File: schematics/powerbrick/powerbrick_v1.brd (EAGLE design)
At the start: 100 x 80 mm, 39 parts, among them U1 ATXMEGA128C3-AU, U2 TC1262-3.3VDB, U3 PRTR5V0U2X, U4 ULN2003LVPWR, U5 MCP9800A0T-M/OT

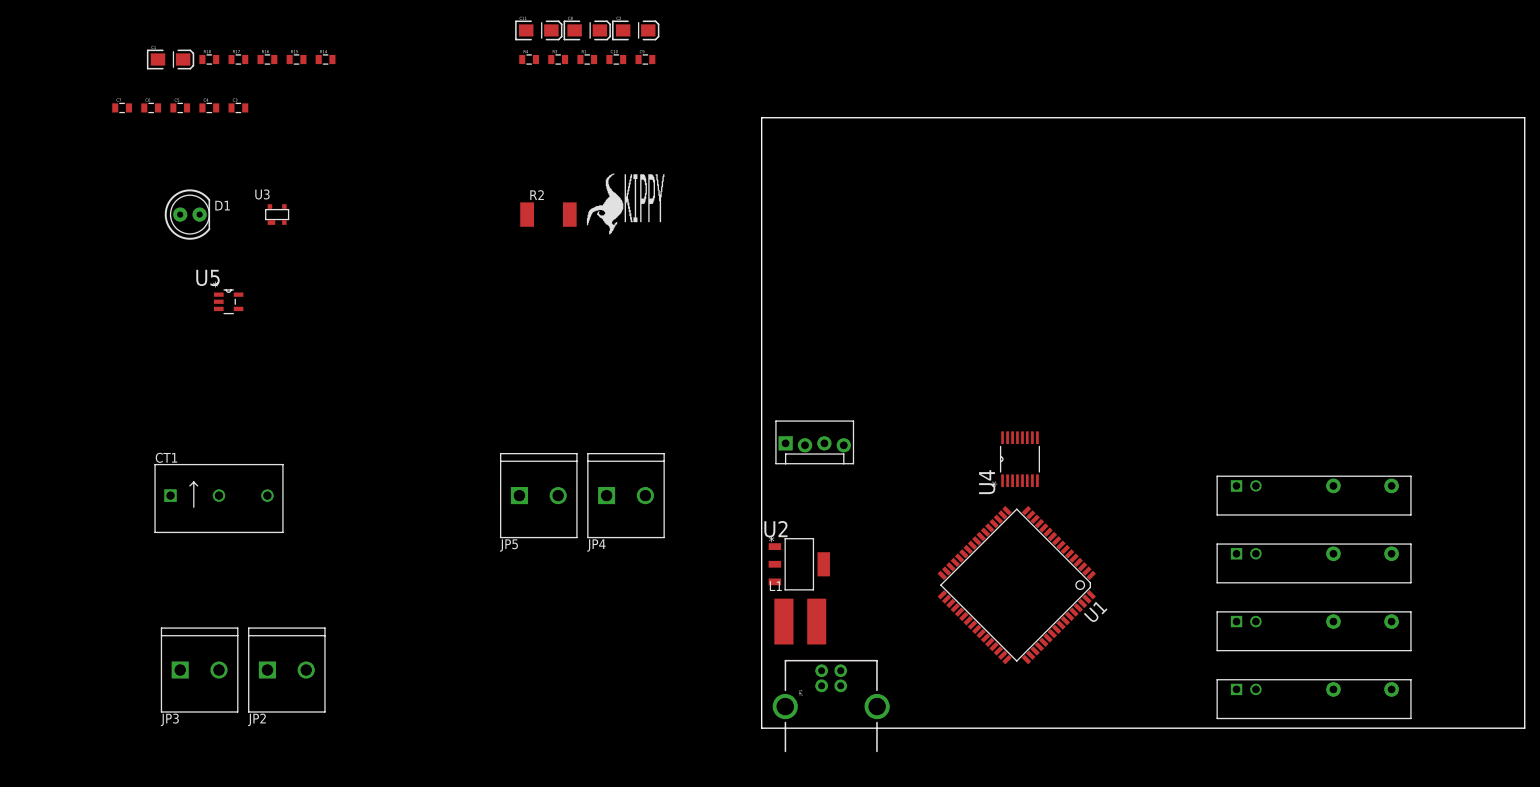
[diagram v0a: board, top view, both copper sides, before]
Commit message: Added ISP header
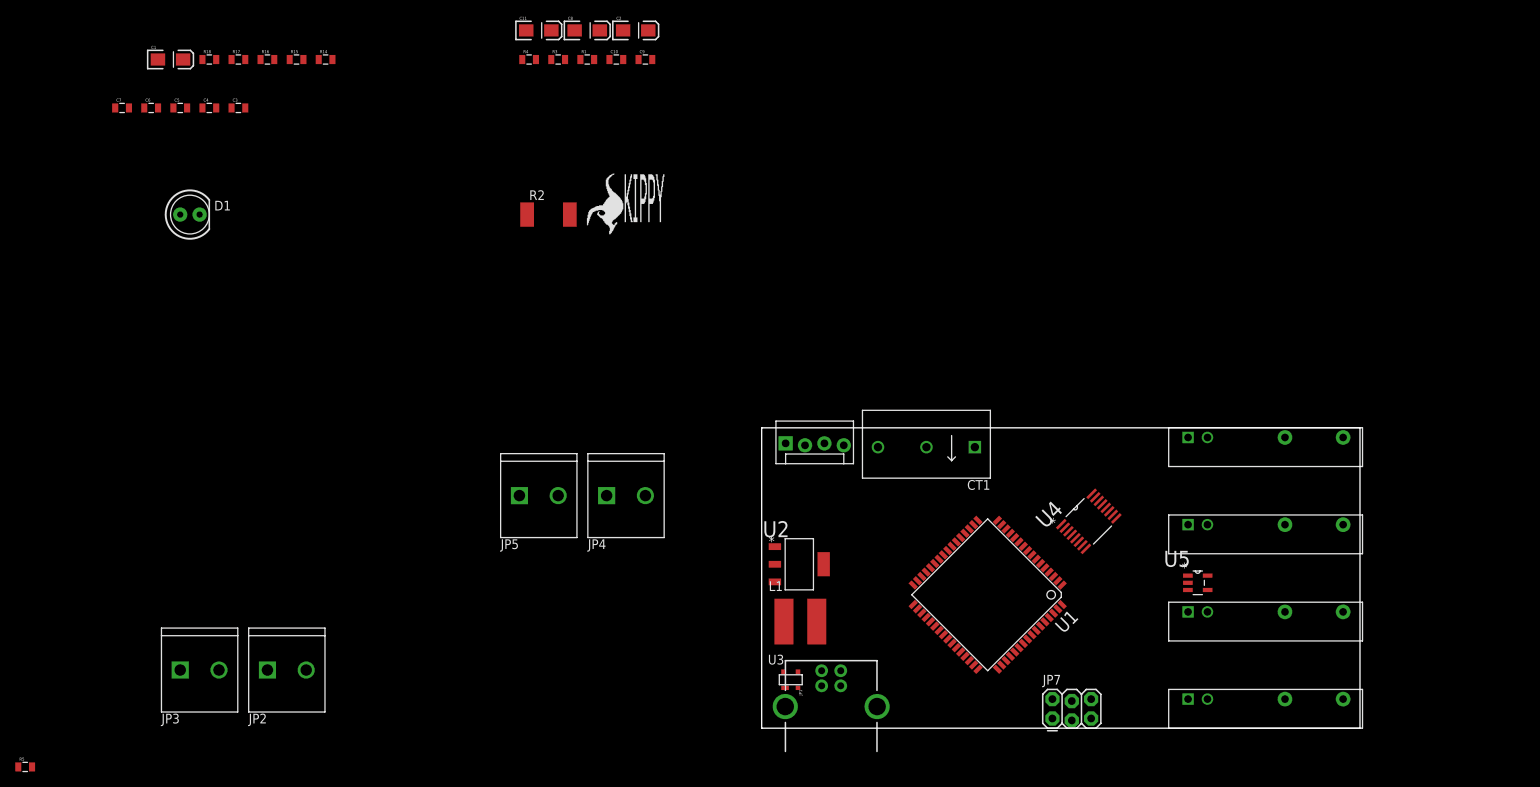
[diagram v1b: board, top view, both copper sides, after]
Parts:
- added JP7: AVR_SPI_PRG_62X3_LOCK, SparkFun-Connectors:2X3_LOCK
- added R5: 10k, SparkFun-Passives:0805
- moved U5 132.2 mm to (57.1, 19.1)
- moved CT1 92.9 mm to (21.6, 36.8), turned to 180 degrees
- moved U3 90.8 mm to (3.81, 6.35)
- moved SSR3 17.7 mm to (66.0, 15.2)
- moved SSR1 16.5 mm to (66.0, 38.1)
- moved SSR2 14.2 mm to (66.0, 26.7)
- moved U4 12.1 mm to (42.9, 27.1), turned to 45 degrees
- moved SSR4 6.48 mm to (66.0, 3.81)
- moved U1 4.02 mm to (29.6, 17.5)
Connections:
- new net PDI_CLK: JP7.5, R5.2, U1.57
- new net PDI_DATA: JP7.1, U1.56
- net 3.3V: now also JP7.2, R5.1
- net GND: now also JP7.6
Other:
- board size 100 x 80 mm -> 78.4 x 39.4 mm

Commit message: Replaced ISP connector - PCB draft
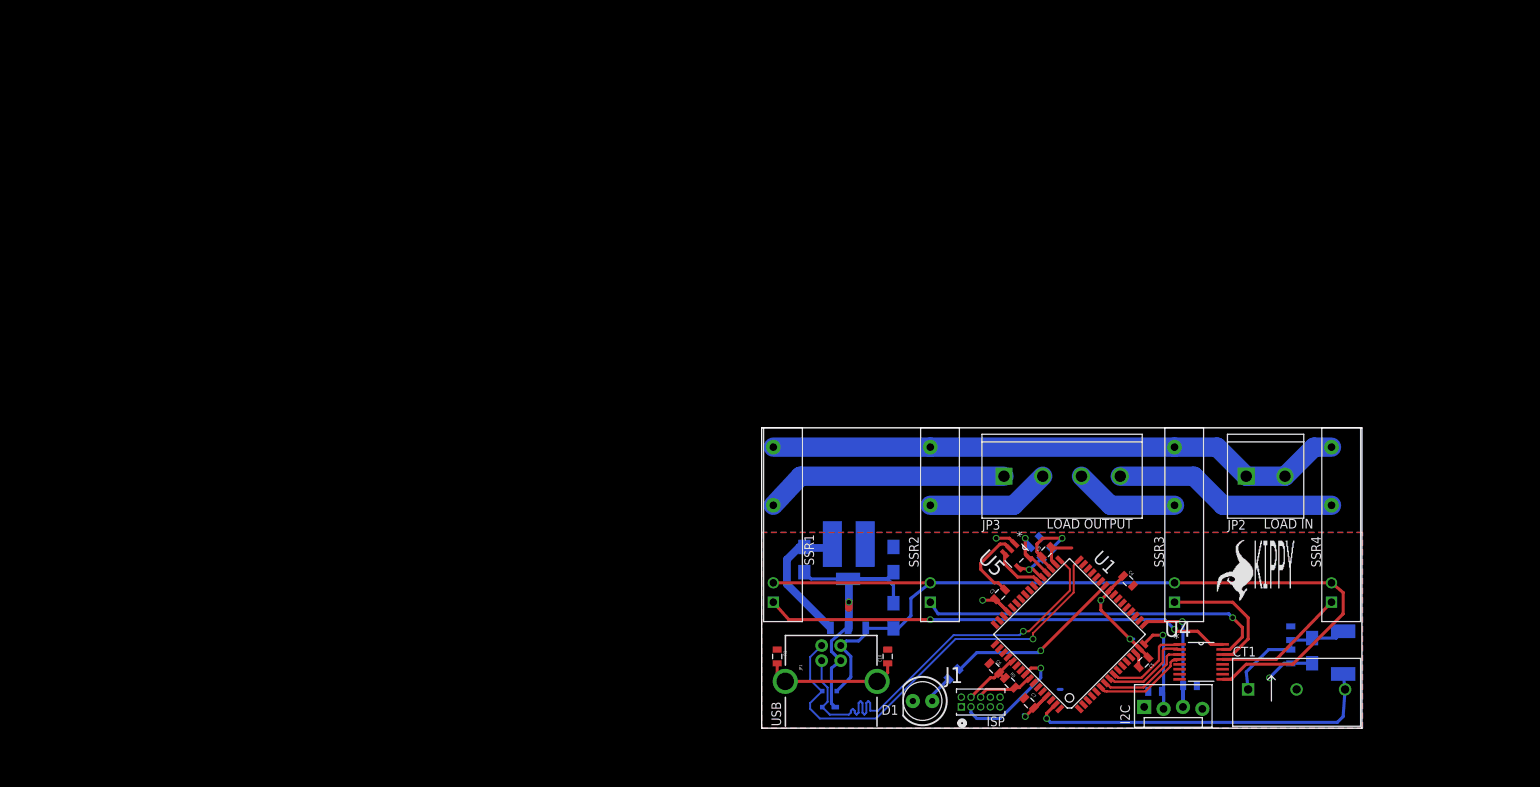
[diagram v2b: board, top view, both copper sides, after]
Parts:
- removed JP4, JP5: SCREW-X2-5.08MM, Skippy-Connectors:1X02-5.08MM
- removed JP7: AVR_SPI_PRG_62X3_LOCK, SparkFun-Connectors:2X3_LOCK
- added J1: FTS-105-01-L-D, Skippy-Connectors:SAMTEC_FTS-105-01-L-D
- JP3: value SCREW-X2-5.08MM -> SCREW-X4-5.08MM; device Skippy-Connectors:1X02-5.08MM -> Skippy-Connectors:1X04
- moved R18 152.5 mm to (56.1, 5.59), flipped to the bottom
- moved R17 145.9 mm to (51.6, 4.83), flipped to the bottom, turned to 180 degrees
- moved C5 145.6 mm to (50.0, 8.64), turned to 225 degrees
- moved C7 142.2 mm to (35.1, 3.30), turned to 135 degrees
- moved C4 135.4 mm to (48.0, 19.3), turned to 315 degrees
- moved C6 132.7 mm to (30.5, 7.87), turned to 135 degrees
- moved JP2 130.8 mm to (66.0, 33.0)
- moved C11 129.9 mm to (72.1, 10.2), flipped to the bottom, turned to 90 degrees
- moved R5 129.5 mm to (32.5, 5.95), turned to 315 degrees
- moved R4 126.8 mm to (69.3, 9.40), flipped to the bottom, turned to 90 degrees
- moved R3 121.9 mm to (69.3, 12.4), flipped to the bottom, turned to 90 degrees
- moved R16 120.9 mm to (37.3, 22.9), flipped to the bottom, turned to 315 degrees
- moved C1 119.5 mm to (17.3, 14.7), flipped to the bottom, turned to 270 degrees
- moved R2 118.9 mm to (76.2, 9.91), flipped to the bottom, turned to 270 degrees
- moved C3 118.4 mm to (31.2, 17.5), turned to 45 degrees
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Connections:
- removed net IN2: JP3.P$1, SSR2.P$4
- removed net IN3: JP4.P$1, SSR3.P$4
- removed net IN4: JP5.P$1, SSR4.P$4
- net 3.3V: now also J1.4; no longer JP7.2
- net GND: now also J1.2, U3.1; no longer JP7.6
- net IN1: now also JP2.P$2, SSR2.P$4, SSR3.P$4, SSR4.P$4
- net OUT1: now also JP3.P$1; no longer JP2.P$2
- net OUT3: now also JP3.P$3; no longer JP4.P$2
- net OUT4: now also JP3.P$4; no longer JP5.P$2
- net PDI_CLK: now also J1.6; no longer JP7.5
- net PDI_DATA: now also J1.3; no longer JP7.1
- net VCC: now also U3.4, U4.9
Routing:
- net VCC: track 0.00 -> 121.7 mm
- net IN1: track 0.00 -> 76.3 mm
- net GND: track 0.00 -> 68.8 mm, vias 0 -> 2
- net CTRL_1: track 0.00 -> 61.3 mm, vias 0 -> 2
- net USB_DM: track 0.00 -> 57.2 mm, vias 0 -> 1
- net USB_DP: track 0.00 -> 57.2 mm, vias 0 -> 1
- net 3.3V: track 0.00 -> 50.6 mm, vias 0 -> 6
- net CURRENT_1: track 0.00 -> 47.3 mm, vias 0 -> 1
- net CTRL_2: track 0.00 -> 47.0 mm, vias 0 -> 1
- net OUT1: track 0.00 -> 31.9 mm
- net OUT4: track 0.00 -> 29.3 mm
- net N$11: track 0.00 -> 23.8 mm, vias 0 -> 1
- net SCL0: track 0.00 -> 19.2 mm, vias 0 -> 1
- net N$2: track 0.00 -> 18.3 mm
- net N$4: track 0.00 -> 17.9 mm
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- added copper zone on layer 16, net 3.3V
- added copper zone on layer 1, net GND
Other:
- board size 78.4 x 39.4 mm -> 78.7 x 39.4 mm
- board text added: "I2C"
- board text added: "ISP"
- board text added: "LOAD IN"
- board text added: "LOAD OUTPUT"
- board text added: "SSR1"
- board text added: "SSR2"
- board text added: "SSR3"
- board text added: "SSR4"
- board text added: "USB"

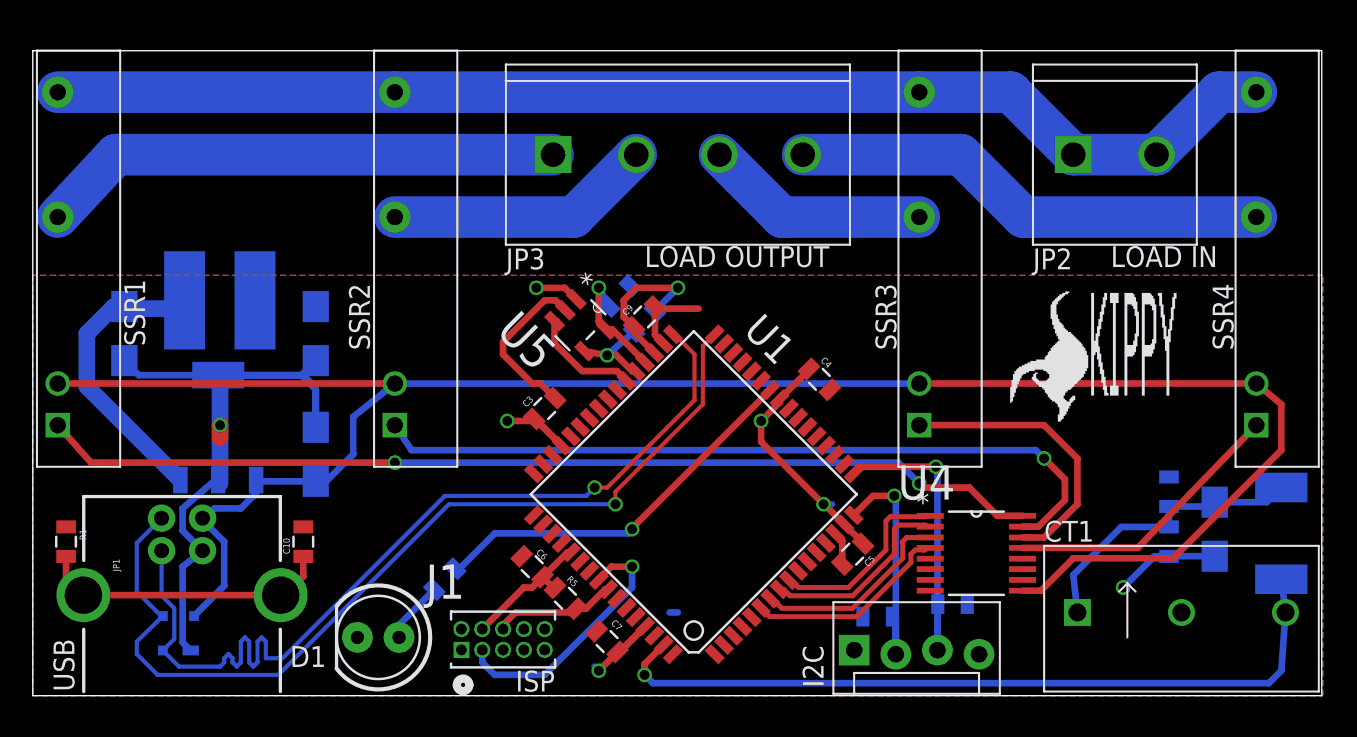
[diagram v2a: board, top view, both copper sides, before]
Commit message: Added test points and HV separation milling
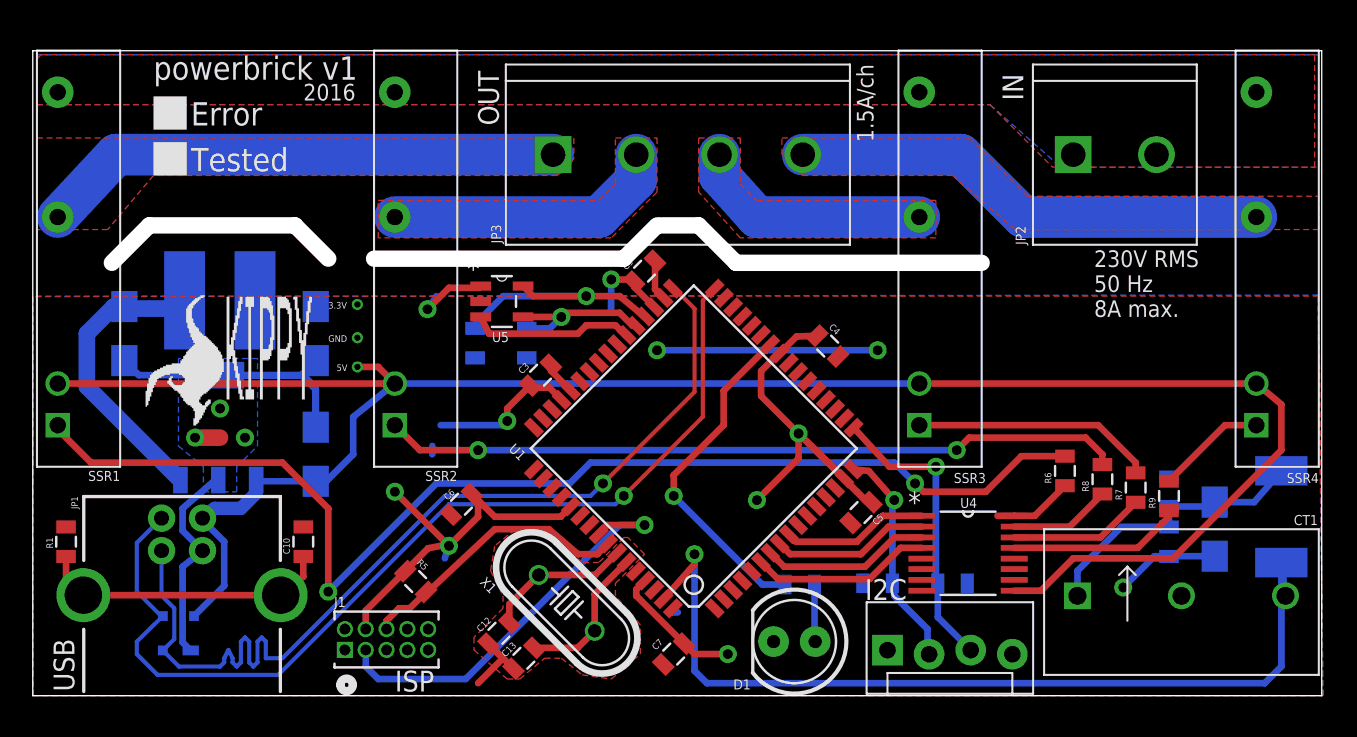
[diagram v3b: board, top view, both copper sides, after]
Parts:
- added C12, C13: 18p, SparkFun-Capacitors:0805
- added R6, R7, R8, R9: Unfit, SparkFun-Passives:0805
- added TP1, TP2, TP3: TEST-POINTTP_15TH_THRU, SparkFun-Passives:TP_15TH
- added X1: 16MHz, Discrete:HC49S
- moved U$2 52.8 mm to (6.93, 16.5)
- moved D1 25.4 mm to (46.5, 3.30)
- moved R14 21.7 mm to (46.8, 6.78), turned to 0 degrees
- moved R15 9.27 mm to (27.0, 21.5), turned to 90 degrees
- moved R5 9.20 mm to (23.4, 6.96)
- moved R16 7.31 mm to (30.2, 21.5), turned to 90 degrees
- moved J1 7.11 mm to (24.1, 4.06)
- moved C6 5.76 mm to (26.2, 11.7), turned to 225 degrees
- moved U5 5.01 mm to (28.6, 24.1), turned to 0 degrees
- moved C7 4.13 mm to (39.1, 2.54), turned to 225 degrees
- moved C9 2.79 mm to (37.3, 25.9)
- moved U1 2.79 mm to (40.3, 15.1)
- moved C5 2.59 mm to (50.5, 11.2)
- moved C4 2.09 mm to (48.5, 21.3)
- moved C3 2.05 mm to (31.0, 19.6)
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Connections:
- new net N$1: C12.2, U1.58, X1.2
- new net N$10: R9.2, SSR4.P$1
- new net N$13: R8.2, SSR2.P$1
- new net N$3: C13.2, U1.59, X1.1
- new net N$6: R6.2, SSR1.P$1
- new net N$9: R7.2, SSR3.P$1
- net 3.3V: now also TP2.P$1
- net CTRL_1: now also R6.1; no longer SSR1.P$1
- net CTRL_2: now also R8.1; no longer SSR2.P$1
- net CTRL_3: now also R7.1; no longer SSR3.P$1
- net CTRL_4: now also R9.1; no longer SSR4.P$1
- net GND: now also C12.1, C13.1, TP3.P$1
- net VCC: now also TP1.P$1
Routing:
- net IN1: track 76.3 -> 0.00 mm
- net N$6: track 0.00 -> 73.7 mm, vias 0 -> 2
- net CTRL_1: track 61.3 -> 4.88 mm, vias 2 -> 0
- net N$13: track 0.00 -> 45.2 mm, vias 0 -> 2
- net CTRL_2: track 47.0 -> 6.20 mm, vias 1 -> 0
- net 3.3V: track 50.6 -> 79.7 mm, vias 6 -> 8
- net N$9: track 0.00 -> 14.8 mm
- net PDI_CLK: track 7.56 -> 17.1 mm
- net PDI_DATA: track 16.1 -> 25.3 mm
- net CTRL_3: track 17.5 -> 8.30 mm
- net N$3: track 0.00 -> 9.12 mm
- net N$1: track 0.00 -> 9.02 mm
- net SDA1: track 7.23 -> 15.9 mm
- net CURRENT_1: track 47.3 -> 55.5 mm
- net CTRL_4: track 17.4 -> 10.6 mm
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- added copper zone on layer 16, net GND
- added copper zone on layer 1, net IN1
- added copper zone on layer 16, net IN1
- added copper zone on layer 1, net OUT1
- added copper zone on layer 1, net OUT2
- added copper zone on layer 1, net OUT3
- added copper zone on layer 1, net OUT4
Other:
- outline, holes or cut-outs redrawn
- board text added: "1.5A/ch"
- board text added: "2016"
- board text added: "230V RMS 50 Hz 8A max."
- board text added: "3.3V"
- board text added: "5V"
- board text added: "Error"
- board text added: "GND"
- board text added: "IN"
- board text added: "OUT"
- board text added: "Tested"
- board text added: "powerbrick v1"
- board text removed: "LOAD IN"
- board text removed: "LOAD OUTPUT"

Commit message: Added slots to separate power planes from mains voltage traces
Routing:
- net USB_DP: track 60.1 -> 58.4 mm
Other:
- outline, holes or cut-outs redrawn
- board text added: "3 slots without copper"
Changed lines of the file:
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@@
 <wire x1="38.1" y1="28.702" x2="36.068" y2="26.67" width="1" layer="46"/>
 <wire x1="36.068" y1="26.67" x2="20.828" y2="26.67" width="1" layer="46"/>
-<wire x1="38.354" y1="28.702" x2="40.64" y2="28.702" width="1" layer="46"/>
 <wire x1="40.64" y1="28.702" x2="42.926" y2="26.416" width="1" layer="46"/>
 <wire x1="42.926" y1="26.416" x2="57.912" y2="26.416" width="1" layer="46"/>
+<text x="18.034" y="20.32" size="1.778" layer="46">3 slots without copper</text>
+<wire x1="17.78" y1="21.336" x2="14.478" y2="21.336" width="0.254" layer="46"/>
+<wire x1="14.478" y1="21.336" x2="14.478" y2="25.654" width="0.254" layer="46"/>
+<wire x1="14.478" y1="25.654" x2="13.716" y2="24.892" width="0.254" layer="46"/>
+<wire x1="14.478" y1="25.654" x2="15.24" y2="24.892" width="0.254" layer="46"/>
+<wire x1="30.988" y1="22.352" x2="30.988" y2="24.638" width="0.254" layer="46"/>
+<wire x1="30.988" y1="24.638" x2="30.226" y2="24.13" width="0.254" layer="46"/>
+<wire x1="30.988" y1="24.638" x2="31.75" y2="24.13" width="0.254" layer="46"/>
+<wire x1="42.672" y1="21.082" x2="48.006" y2="21.082" width="0.254" layer="46"/>
+<wire x1="48.006" y1="21.082" x2="48.006" y2="24.384" width="0.254" layer="46"/>
+<wire x1="48.006" y1="24.384" x2="47.244" y2="23.622" width="0.254" layer="46"/>
+<wire x1="48.006" y1="24.384" x2="48.768" y2="23.622" width="0.254" layer="46"/>
 </plain>
 <attributes>
@@
 <wire x1="25.146" y1="12.192" x2="15.24" y2="2.286" width="0.254" layer="16"/>
 <wire x1="8.922" y1="1.778" x2="7.94" y2="2.76" width="0.254" layer="16"/>
-<wire x1="15.24" y1="2.286" x2="14.224" y2="2.286" width="0.254" layer="16"/>
-<wire x1="14.224" y1="2.286" x2="14.224" y2="3.302" width="0.254" layer="16"/>
-<wire x1="14.224" y1="3.302" x2="13.97" y2="3.556" width="0.254" layer="16"/>
-<wire x1="13.97" y1="3.556" x2="13.716" y2="3.302" width="0.254" layer="16"/>
 <wire x1="13.716" y1="3.302" x2="13.716" y2="2.032" width="0.254" layer="16"/>
-<wire x1="13.716" y1="2.032" x2="13.462" y2="1.778" width="0.254" layer="16"/>
-<wire x1="13.462" y1="1.778" x2="13.208" y2="2.032" width="0.254" layer="16"/>
 <wire x1="13.208" y1="2.032" x2="13.208" y2="3.302" width="0.254" layer="16"/>
-<wire x1="13.208" y1="3.302" x2="12.954" y2="3.556" width="0.254" layer="16"/>
-<wire x1="12.954" y1="3.556" x2="12.7" y2="3.302" width="0.254" layer="16"/>
 <wire x1="12.7" y1="3.302" x2="12.7" y2="2.032" width="0.254" layer="16"/>
-<wire x1="12.7" y1="2.032" x2="12.446" y2="1.778" width="0.254" layer="16"/>
 <wire x1="11.43" y1="1.778" x2="8.922" y2="1.778" width="0.254" layer="16"/>
-<wire x1="12.446" y1="1.778" x2="12.192" y2="2.032" width="0.254" layer="16"/>
 <wire x1="12.192" y1="2.032" x2="12.192" y2="2.286" width="0.254" layer="16"/>
-<wire x1="12.192" y1="2.286" x2="11.938" y2="2.794" width="0.254" layer="16"/>
-<wire x1="11.938" y1="2.794" x2="11.684" y2="2.286" width="0.254" layer="16"/>
 <wire x1="11.684" y1="2.286" x2="11.684" y2="2.032" width="0.254" layer="16"/>
-<wire x1="11.684" y1="2.032" x2="11.43" y2="1.778" width="0.254" layer="16"/>
 <wire x1="34.036" y1="12.192" x2="34.798" y2="12.954" width="0.254" layer="16"/>
 <via x="34.798" y="12.954" extent="1-16" drill="0.6"/>
@@
 <wire x1="40.386" y1="23.622" x2="39.165928125" y2="24.842071875" width="0.254" layer="1"/>
 <wire x1="39.165928125" y1="24.842071875" x2="39.06720625" y2="24.842071875" width="0.254" layer="1"/>
+<wire x1="14.224" y1="3.302" x2="13.716" y2="3.302" width="0.254" layer="16" curve="180"/>
+<wire x1="13.716" y1="2.032" x2="13.208" y2="2.032" width="0.254" layer="16" curve="-180"/>
+<wire x1="13.208" y1="3.302" x2="12.7" y2="3.302" width="0.254" layer="16" curve="180"/>
+<wire x1="12.7" y1="2.032" x2="12.192" y2="2.032" width="0.254" layer="16" curve="-180"/>
+<wire x1="12.192" y1="2.286" x2="11.684" y2="2.286" width="0.254" layer="16" curve="180"/>
+<wire x1="11.684" y1="2.032" x2="11.43" y2="1.778" width="0.254" layer="16" curve="-90"/>
+<wire x1="15.24" y1="2.286" x2="14.224" y2="2.54" width="0.254" layer="16" curve="-118.072487"/>
+<wire x1="14.224" y1="2.54" x2="14.224" y2="3.302" width="0.254" layer="16"/>
 </signal>
 <signal name="USB_DM">
